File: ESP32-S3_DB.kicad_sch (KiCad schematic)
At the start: 1 part, among them U1 ESP32-S3

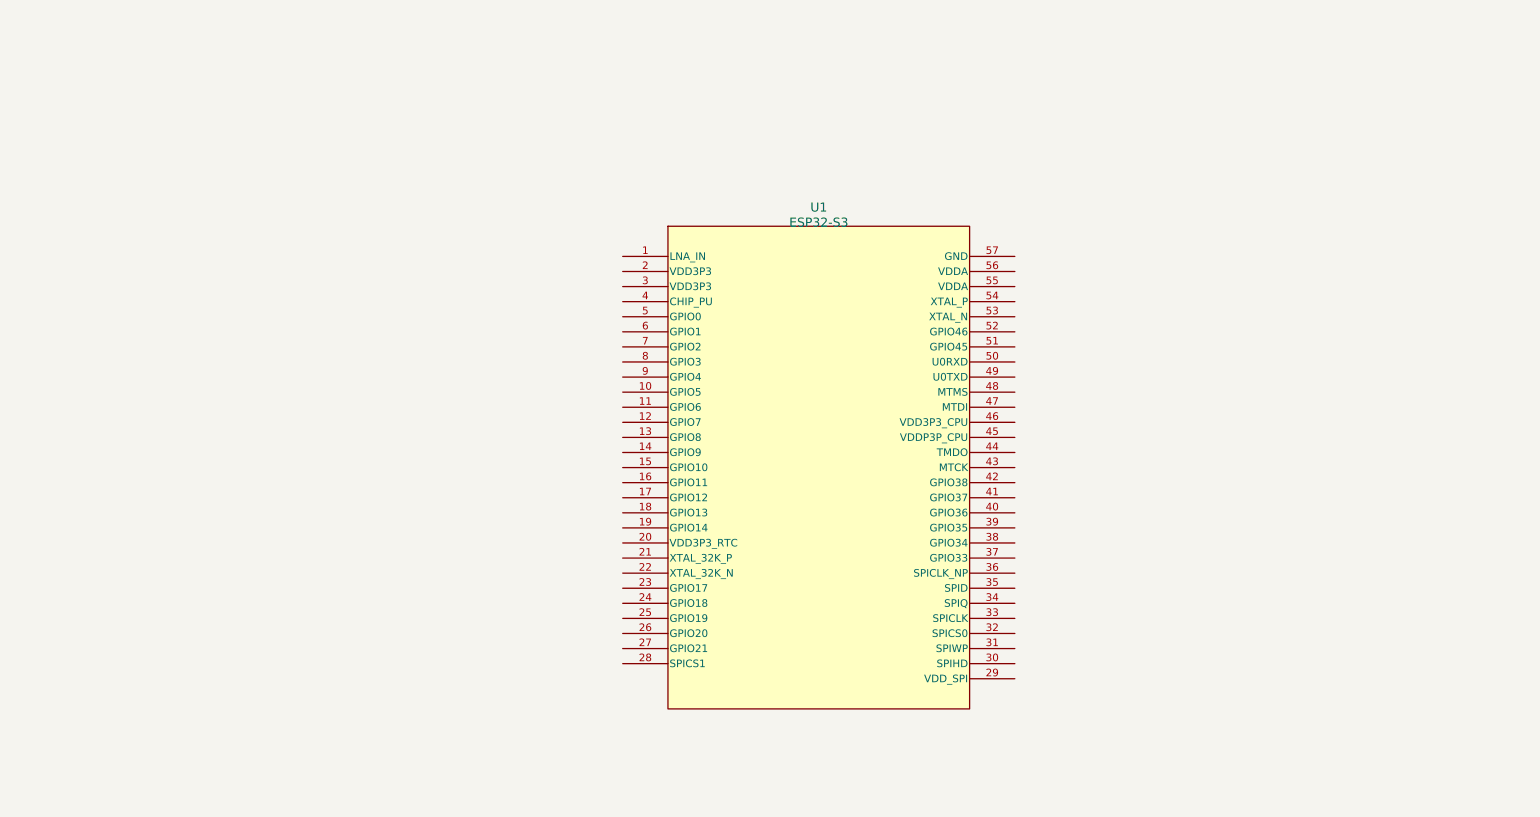
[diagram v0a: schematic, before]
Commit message: Started designed the schematics
Placed passives for supply pins and antenna
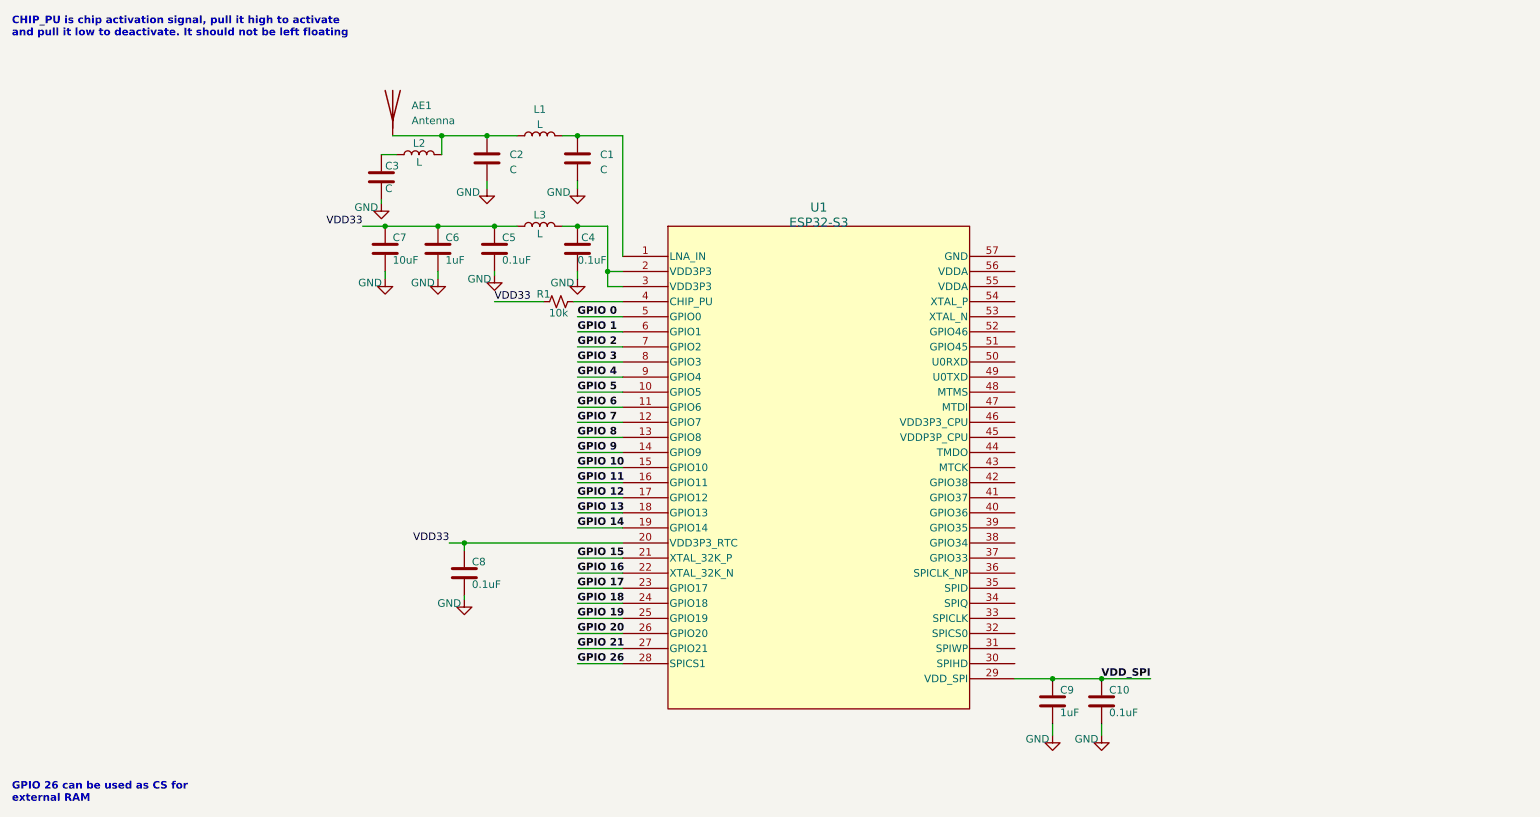
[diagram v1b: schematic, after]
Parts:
- added AE1: Antenna, symbol ESP32-S3_DB:Antenna
- added C1, C2, C3: C, symbol ESP32-S3_DB:C
- added C10, C4, C5, C8: 0.1uF, symbol ESP32-S3_DB:C
- added C6, C9: 1uF, symbol ESP32-S3_DB:C
- added C7: 10uF, symbol ESP32-S3_DB:C
- added L1, L2, L3: L, symbol ESP32-S3_DB:L
- added R1: 10k, symbol ESP32-S3_DB:R_Small_US
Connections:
- net at U1.1 (LNA_IN): now also C1.1, L1.2
- net GPIO 5: now reaches U1.10 (GPIO5)
- net GPIO 6: now reaches U1.11 (GPIO6)
- net GPIO 7: now reaches U1.12 (GPIO7)
- net GPIO 8: now reaches U1.13 (GPIO8)
- net GPIO 9: now reaches U1.14 (GPIO9)
- net GPIO 10: now reaches U1.15 (GPIO10)
- net GPIO 11: now reaches U1.16 (GPIO11)
- net GPIO 12: now reaches U1.17 (GPIO12)
- net GPIO 13: now reaches U1.18 (GPIO13)
- net GPIO 14: now reaches U1.19 (GPIO14)
- net at U1.2 (VDD3P3): now also U1.3 (VDD3P3), C4.1, L3.2
- net VDD33: now reaches U1.20 (VDD3P3_RTC)
- net VDD33: now also C5.1, C6.1, C7.1, C8.1, L3.1, R1.1
- net GPIO 15: now reaches U1.21 (XTAL_32K_P)
- net GPIO 16: now reaches U1.22 (XTAL_32K_N)
- net GPIO 17: now reaches U1.23 (GPIO17)
- net GPIO 18: now reaches U1.24 (GPIO18)
- net GPIO 19: now reaches U1.25 (GPIO19)
- net GPIO 20: now reaches U1.26 (GPIO20)
- net GPIO 21: now reaches U1.27 (GPIO21)
- net GPIO 26: now reaches U1.28 (SPICS1)
- net VDD_SPI: now reaches U1.29 (VDD_SPI)
- net VDD_SPI: now also C10.1, C9.1
- net at U1.4 (CHIP_PU): now also R1.2
- net GPIO 0: now reaches U1.5 (GPIO0)
- net GPIO 1: now reaches U1.6 (GPIO1)
- net GPIO 2: now reaches U1.7 (GPIO2)
- net GPIO 3: now reaches U1.8 (GPIO3)
- net GPIO 4: now reaches U1.9 (GPIO4)
- new net: AE1.1 (A), C2.1, L1.1, L2.2
- new net: C3.1, L2.1
- new net GND: C1.2, C10.2, C2.2, C3.2, C4.2, C5.2, C6.2, C7.2, C8.2, C9.2
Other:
- note added: "CHIP_PU is chip activation signal, pull it high to activate and pull it low to deactivate. It should not be left floating"
- note added: "GPIO 26 can be used as CS for external RAM"

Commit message: Added External Flash and Power sheets
Added External Flash and Power sheets. Finished adding all the passives at their respective pins. Incorrect Pin number and signal corrected.
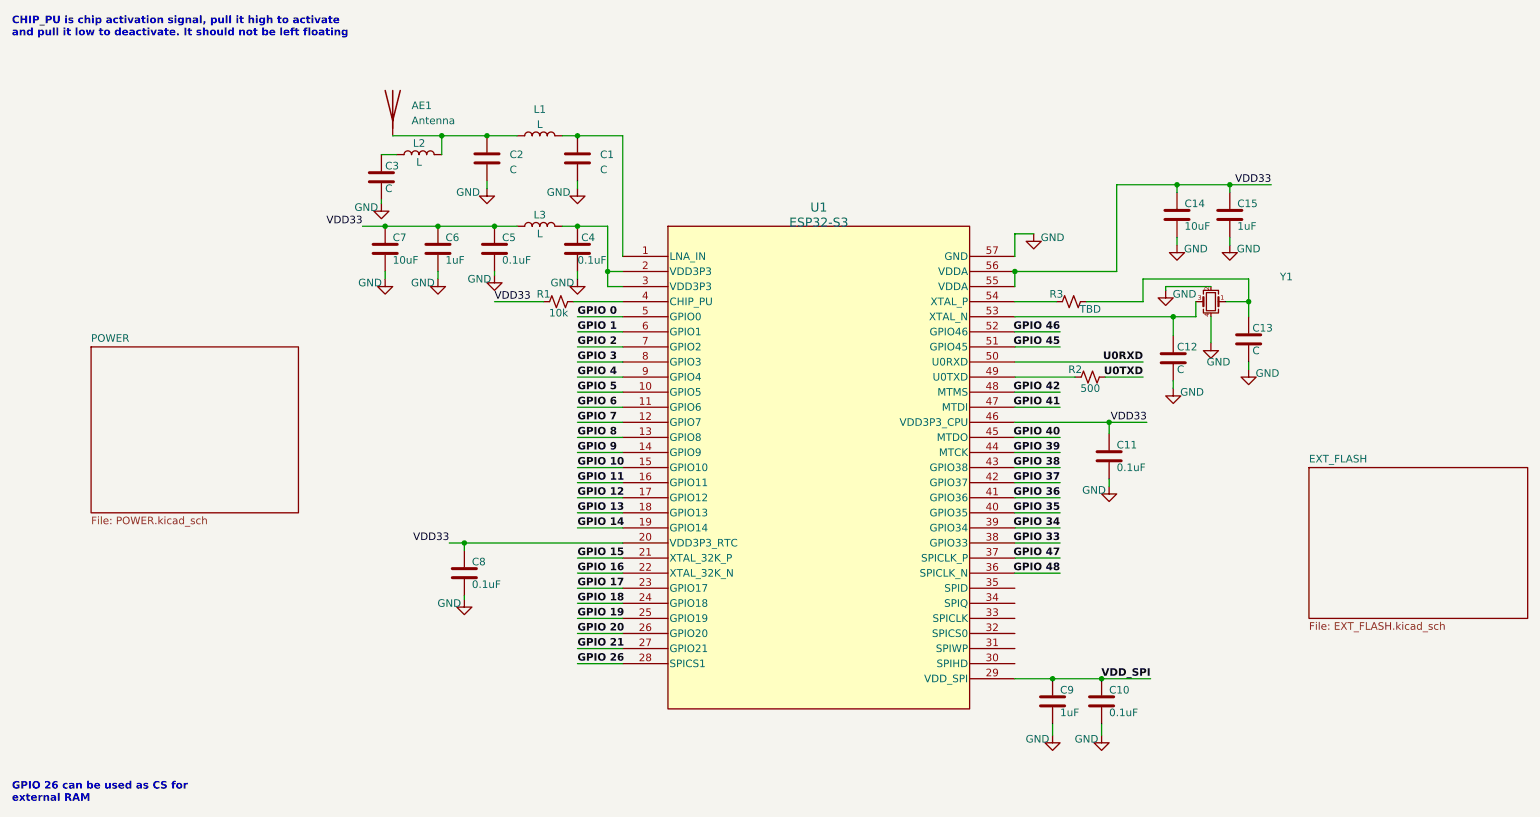
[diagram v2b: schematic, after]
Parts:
- added C11: 0.1uF, symbol ESP32-S3_DB:C
- added C12, C13: C, symbol ESP32-S3_DB:C
- added C14: 10uF, symbol ESP32-S3_DB:C
- added C15: 1uF, symbol ESP32-S3_DB:C
- added R2: 500, symbol ESP32-S3_DB:R_Small_US
- added R3: TBD, symbol ESP32-S3_DB:R_Small_US
- added Y1: Crystal_GND24_Small, symbol ESP32-S3_DB:Crystal_GND24_Small
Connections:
- net GND: now also U1.57 (GND), C11.2, C12.2, C13.2, C14.2, C15.2, Y1.2, Y1.4
- net VDD33: now also U1.46 (VDD3P3_CPU), U1.55 (VDDA), U1.56 (VDDA), C11.1, C14.1, C15.1
- net GPIO 48: now reaches U1.36 (SPICLK_N)
- net GPIO 47: now reaches U1.37 (SPICLK_P)
- net GPIO 33: now reaches U1.38 (GPIO33)
- net GPIO 34: now reaches U1.39 (GPIO34)
- net GPIO 35: now reaches U1.40 (GPIO35)
- net GPIO 36: now reaches U1.41 (GPIO36)
- net GPIO 37: now reaches U1.42 (GPIO37)
- net GPIO 38: now reaches U1.43 (GPIO38)
- net GPIO 39: now reaches U1.44 (MTCK)
- net GPIO 40: now reaches U1.45 (MTDO)
- net GPIO 41: now reaches U1.47 (MTDI)
- net GPIO 42: now reaches U1.48 (MTMS)
- net at U1.49 (U0TXD): now also R2.1
- net U0RXD: now reaches U1.50 (U0RXD)
- net GPIO 45: now reaches U1.51 (GPIO45)
- net GPIO 46: now reaches U1.52 (GPIO46)
- net at U1.53 (XTAL_N): now also C12.1, Y1.3
- net at U1.54 (XTAL_P): now also R3.1
- new net: C13.1, R3.2, Y1.1
- new net U0TXD: R2.2
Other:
- added sheet EXT_FLASH (EXT_FLASH.kicad_sch)
- added sheet POWER (POWER.kicad_sch)

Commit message: Created Block arrangement and added USB C connector
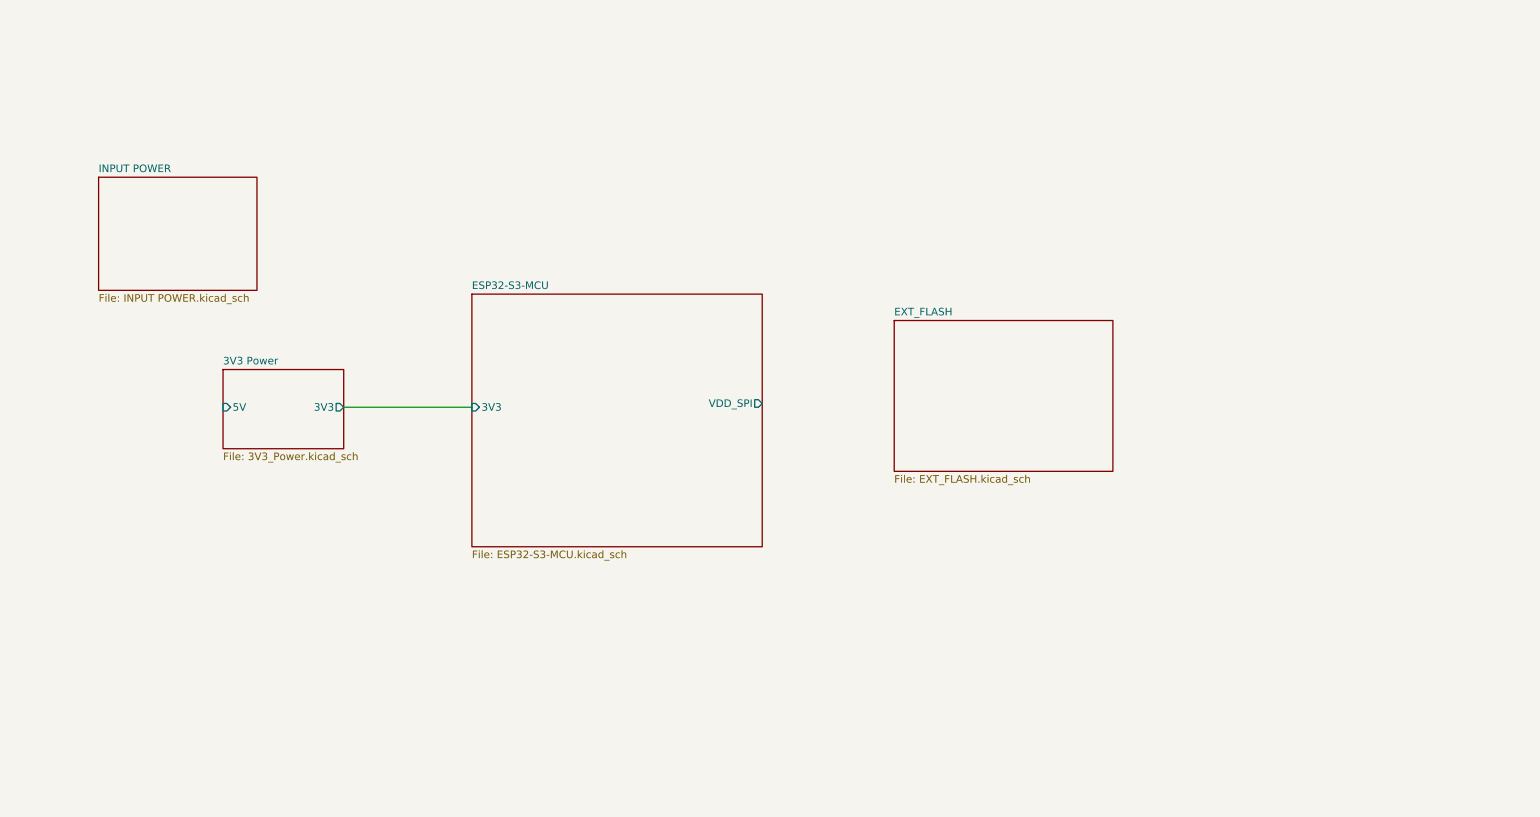
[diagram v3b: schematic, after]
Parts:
- removed AE1: Antenna, symbol ESP32-S3_DB:Antenna
- removed C1, C12, C13, C2, C3: C, symbol ESP32-S3_DB:C
- removed C10, C11, C4, C5, C8: 0.1uF, symbol ESP32-S3_DB:C
- removed C14, C7: 10uF, symbol ESP32-S3_DB:C
- removed C15, C6, C9: 1uF, symbol ESP32-S3_DB:C
- removed L1, L2, L3: L, symbol ESP32-S3_DB:L
- removed R1: 10k, symbol ESP32-S3_DB:R_Small_US
- removed R2: 500, symbol ESP32-S3_DB:R_Small_US
- removed R3: TBD, symbol ESP32-S3_DB:R_Small_US
- removed U1: ESP32-S3, QFN56_7X7_EXP, symbol ESP32-S3_DB:ESP32-S3
- removed Y1: Crystal_GND24_Small, symbol ESP32-S3_DB:Crystal_GND24_Small
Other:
- sheet POWER renamed 3V3 Power
- added sheet ESP32-S3-MCU (ESP32-S3-MCU.kicad_sch)
- added sheet INPUT POWER (INPUT POWER.kicad_sch)
- sheet 3V3 Power: file POWER.kicad_sch -> 3V3_Power.kicad_sch
- sheet 3V3 Power ports: added 3V3, 5V; removed none
- note removed: "CHIP_PU is chip activation signal, pull it high to activate and pull it low to deactivate. It should not be left floating"
- note removed: "GPIO 26 can be used as CS for external RAM"

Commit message: completed USB-C wiring and added flash
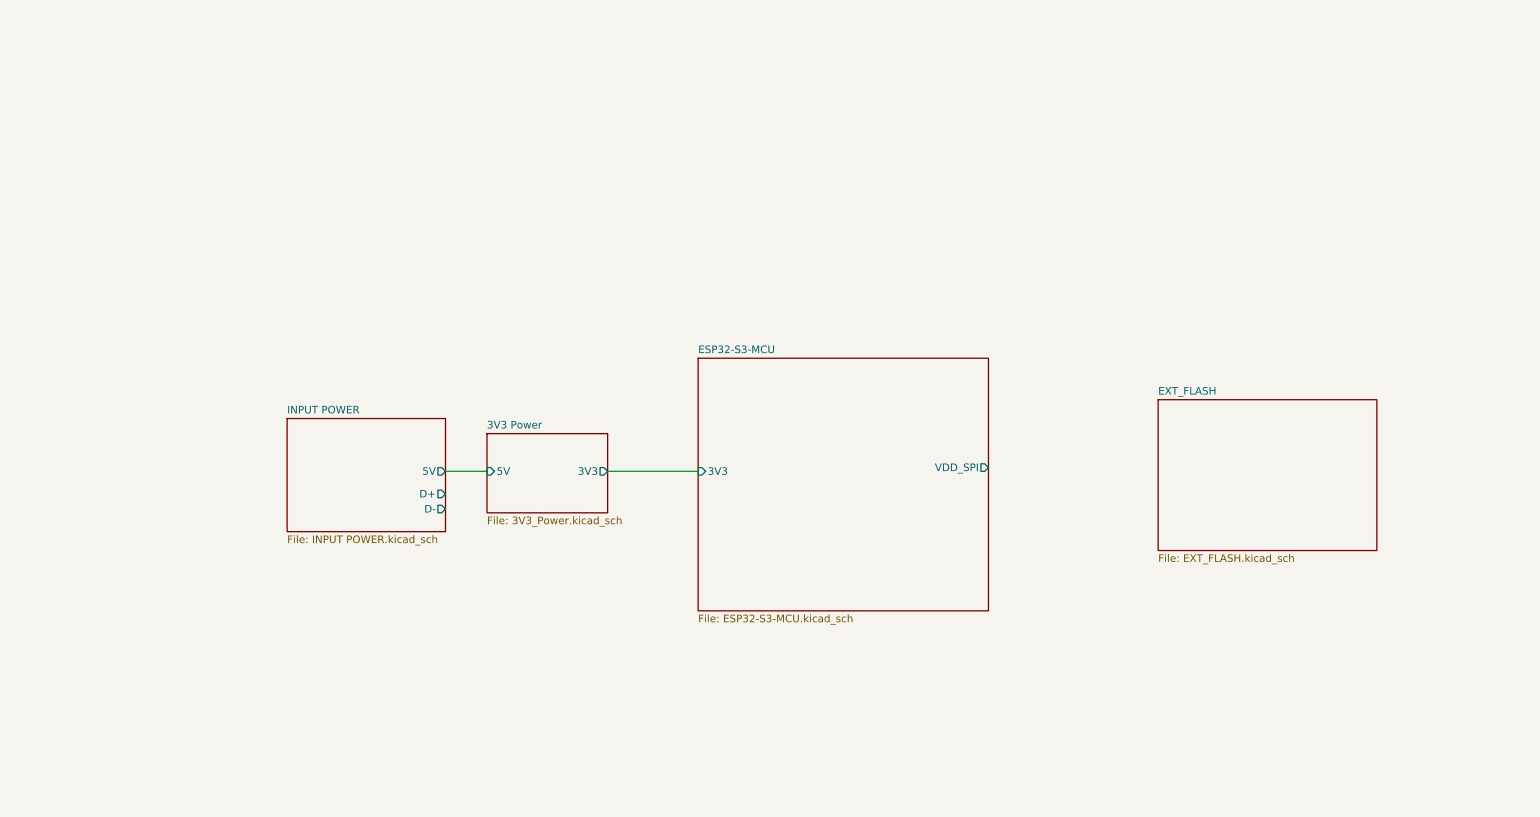
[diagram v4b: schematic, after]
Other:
- sheet INPUT POWER ports: added 5V, D+, D-; removed none
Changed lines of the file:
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@@
 (kicad_sch (version 20230121) (generator eeschema)
   (paper "A4")
-  (wire (pts (xy 73.025 85.725) (xy 94.615 85.725))
+  (wire (pts (xy 90.17 96.52) (xy 97.155 96.52))
     (stroke (width 0) (type default))
   )
-  (sheet (at 165.735 71.12) (size 36.83 25.4) (fields_autoplaced)
+  (wire (pts (xy 117.475 96.52) (xy 132.715 96.52))
+    (stroke (width 0) (type default))
+  )
+  (sheet (at 210.185 84.455) (size 36.83 25.4) (fields_autoplaced)
     (stroke (width 0.1524) (type solid))
     (fill (color 255 255 194 1.0000))
-    (property "Sheetname" "EXT_FLASH" (at 165.735 70.4084 0)
+    (property "Sheetname" "EXT_FLASH" (at 210.185 83.7434 0)
       (effects (font (size 1.27 1.27)) (justify left bottom))
     )
-    (property "Sheetfile" "EXT_FLASH.kicad_sch" (at 165.735 97.1046 0)
+    (property "Sheetfile" "EXT_FLASH.kicad_sch" (at 210.185 110.4396 0)
       (effects (font (size 1.27 1.27)) (justify left top))
     )
@@
     )
   )
-  (sheet (at 31.75 46.99) (size 26.67 19.05) (fields_autoplaced)
+  (sheet (at 63.5 87.63) (size 26.67 19.05) (fields_autoplaced)
     (stroke (width 0.1524) (type solid))
     (fill (color 255 255 194 1.0000))
-    (property "Sheetname" "INPUT POWER" (at 31.75 46.2784 0)
+    (property "Sheetname" "INPUT POWER" (at 63.5 86.9184 0)
       (effects (font (size 1.27 1.27)) (justify left bottom))
     )
-    (property "Sheetfile" "INPUT POWER.kicad_sch" (at 31.75 66.6246 0)
+    (property "Sheetfile" "INPUT POWER.kicad_sch" (at 63.5 107.2646 0)
       (effects (font (size 1.27 1.27)) (justify left top))
+    )
+    (pin "D-" output (at 90.17 102.87 0)
+      (effects (font (size 1.27 1.27)) (justify right))
+    )
+    (pin "D+" output (at 90.17 100.33 0)
+      (effects (font (size 1.27 1.27)) (justify right))
+    )
+    (pin "5V" output (at 90.17 96.52 0)
+      (effects (font (size 1.27 1.27)) (justify right))
     )
     (instances
@@
     )
   )
-  (sheet (at 94.615 66.675) (size 48.895 42.545) (fields_autoplaced)
+  (sheet (at 132.715 77.47) (size 48.895 42.545) (fields_autoplaced)
     (stroke (width 0.1524) (type solid))
     (fill (color 255 255 194 1.0000))
-    (property "Sheetname" "ESP32-S3-MCU" (at 94.615 65.9634 0)
+    (property "Sheetname" "ESP32-S3-MCU" (at 132.715 76.7584 0)
       (effects (font (size 1.27 1.27)) (justify left bottom))
     )
-    (property "Sheetfile" "ESP32-S3-MCU.kicad_sch" (at 94.615 109.8046 0)
+    (property "Sheetfile" "ESP32-S3-MCU.kicad_sch" (at 132.715 120.5996 0)
       (effects (font (size 1.27 1.27)) (justify left top))
     )
-    (pin "3V3" input (at 94.615 85.725 180)
+    (pin "3V3" input (at 132.715 96.52 180)
       (effects (font (size 1.27 1.27)) (justify left))
     )
-    (pin "VDD_SPI" output (at 143.51 85.09 0)
+    (pin "VDD_SPI" output (at 181.61 95.885 0)
       (effects (font (size 1.27 1.27)) (justify right))
     )
@@
     )
   )
-  (sheet (at 52.705 79.375) (size 20.32 13.335) (fields_autoplaced)
+  (sheet (at 97.155 90.17) (size 20.32 13.335) (fields_autoplaced)
     (stroke (width 0.1524) (type solid))
     (fill (color 255 255 194 1.0000))
-    (property "Sheetname" "3V3 Power" (at 52.705 78.6634 0)
+    (property "Sheetname" "3V3 Power" (at 97.155 89.4584 0)
       (effects (font (size 1.27 1.27)) (justify left bottom))
     )
-    (property "Sheetfile" "3V3_Power.kicad_sch" (at 52.705 93.2946 0)
+    (property "Sheetfile" "3V3_Power.kicad_sch" (at 97.155 104.0896 0)
       (effects (font (size 1.27 1.27)) (justify left top))
     )
-    (pin "3V3" output (at 73.025 85.725 0)
+    (pin "3V3" output (at 117.475 96.52 0)
       (effects (font (size 1.27 1.27)) (justify right))
     )
-    (pin "5V" input (at 52.705 85.725 180)
+    (pin "5V" input (at 97.155 96.52 180)
       (effects (font (size 1.27 1.27)) (justify left))
     )
